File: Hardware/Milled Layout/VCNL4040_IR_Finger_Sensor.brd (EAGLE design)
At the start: 14 x 15.2 mm, 9 parts, among them U1 VCNL4040

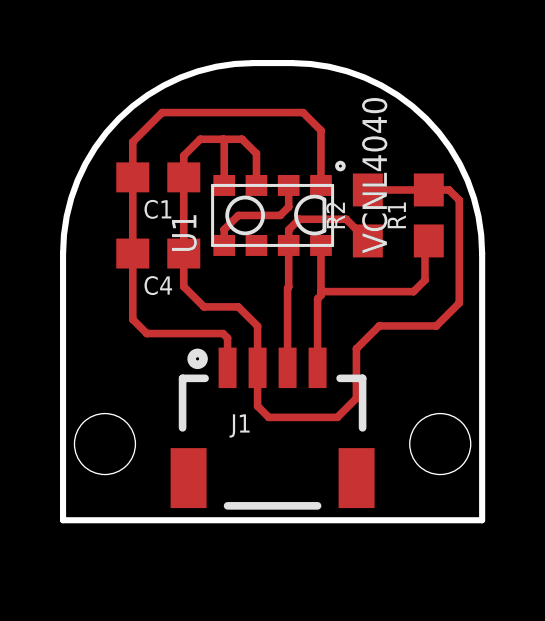
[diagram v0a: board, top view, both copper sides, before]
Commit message: Added a comparison sketch to make sure new IC works similarly to original.
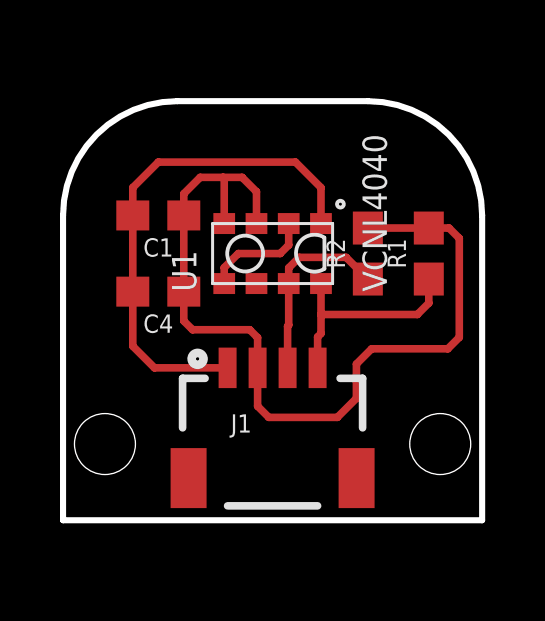
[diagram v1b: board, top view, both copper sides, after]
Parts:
- moved C4 1.27 mm to (3.17, 7.62)
- moved C1 1.27 mm to (3.17, 10.2)
- moved R1 1.27 mm to (12.2, 8.89)
- moved R2 1.27 mm to (10.2, 8.89)
- moved U1 1.27 mm to (6.99, 8.89)
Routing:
- net GND: track 19.1 -> 16.9 mm
- net SCL: track 9.15 -> 7.41 mm
- net 3.3V: track 31.5 -> 29.8 mm
- net SDA: track 7.70 -> 6.43 mm
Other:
- board size 14 x 15.2 mm -> 14 x 14 mm

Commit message: Extending PCB for molding
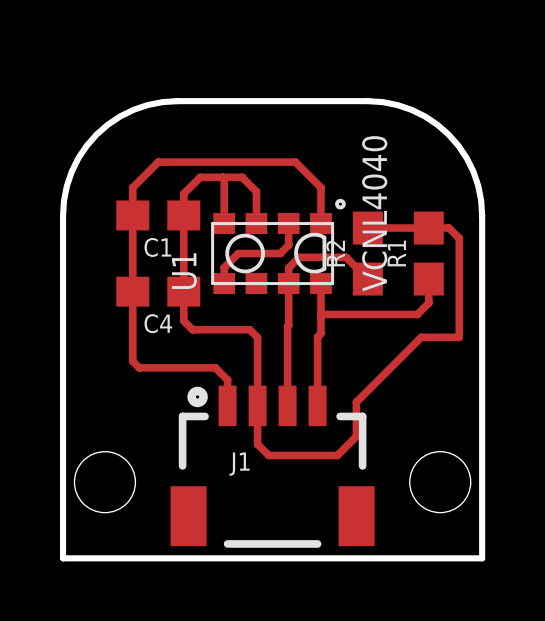
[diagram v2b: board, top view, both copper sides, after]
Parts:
- moved J1 1.27 mm to (6.99, 3.81)
- moved U$1 1.27 mm to (1.40, 1.27)
- moved U$2 1.27 mm to (12.6, 1.27)
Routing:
- net 3.3V: track 29.8 -> 31.6 mm
- net GND: track 16.9 -> 18.2 mm
- net SDA: track 6.43 -> 7.70 mm
- net SCL: track 7.41 -> 8.68 mm
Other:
- board size 14 x 14 mm -> 14 x 15.2 mm
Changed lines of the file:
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@@
 <?xml version="1.0" encoding="utf-8"?>
 <!DOCTYPE eagle SYSTEM "eagle.dtd">
-<eagle version="7.7.0">
+<eagle version="7.6.0">
 <drawing>
 <settings>
@@
 <layer number="47" name="Measures" color="7" fill="1" visible="no" active="yes"/>
 <layer number="48" name="Document" color="7" fill="1" visible="no" active="yes"/>
-<layer number="49" name="Reference" color="7" fill="1" visible="yes" active="yes"/>
+<layer number="49" name="Reference" color="7" fill="1" visible="no" active="yes"/>
 <layer number="50" name="dxf" color="7" fill="1" visible="no" active="no"/>
 <layer number="51" name="tDocu" color="6" fill="1" visible="yes" active="yes"/>
@@
 <board>
 <plain>
-<wire x1="0" y1="0" x2="13.97" y2="0" width="0.2032" layer="20"/>
-<wire x1="0" y1="0" x2="0" y2="10.16" width="0.2032" layer="20"/>
-<wire x1="13.97" y1="10.16" x2="13.97" y2="0" width="0.2032" layer="20"/>
+<wire x1="0" y1="-1.27" x2="13.97" y2="-1.27" width="0.2032" layer="20"/>
+<wire x1="0" y1="-1.27" x2="0" y2="10.16" width="0.2032" layer="20"/>
+<wire x1="13.97" y1="10.16" x2="13.97" y2="-1.27" width="0.2032" layer="20"/>
 <wire x1="10.16" y1="13.97" x2="3.81" y2="13.97" width="0.2032" layer="20"/>
 <text x="16.51" y="5.08" size="1.778" layer="51" font="vector" ratio="15">GooLine</text>
-<wire x1="0" y1="5.08" x2="13.97" y2="5.08" width="0.254" layer="51" style="shortdash"/>
+<wire x1="0" y1="3.81" x2="13.97" y2="3.81" width="0.254" layer="51" style="shortdash"/>
 <wire x1="0" y1="13.97" x2="13.97" y2="13.97" width="0.254" layer="51" style="shortdash"/>
-<wire x1="0" y1="13.97" x2="0" y2="5.08" width="0.254" layer="51" style="shortdash"/>
-<wire x1="13.97" y1="5.08" x2="13.97" y2="13.97" width="0.254" layer="51" style="shortdash"/>
+<wire x1="0" y1="13.97" x2="0" y2="3.81" width="0.254" layer="51" style="shortdash"/>
+<wire x1="13.97" y1="3.81" x2="13.97" y2="13.97" width="0.254" layer="51" style="shortdash"/>
 <dimension x1="0" y1="15.24" x2="13.97" y2="15.24" x3="6.985" y3="16.51" textsize="1.27" textratio="15" layer="47" dtype="horizontal" unit="inch"/>
 <wire x1="0" y1="10.16" x2="3.81" y2="13.97" width="0.2032" layer="20" curve="-90"/>
@@
 </element>
 <element name="U1" library="SparkX" package="VCNL4040" value="VCNL4040" x="6.985" y="8.89" rot="R90"/>
-<element name="U$1" library="SparkX" package="STAND-OFF-#2" value="STAND-OFF" x="1.397" y="2.54"/>
-<element name="U$2" library="SparkX" package="STAND-OFF-#2" value="STAND-OFF" x="12.573" y="2.54"/>
-<element name="J1" library="SparkFun-Connectors" package="1X04_1MM_RA" value="" x="6.985" y="5.08">
-<attribute name="SF_ID" value="PRT-10208" x="6.985" y="5.08" size="1.778" layer="27" font="vector" ratio="15" display="off"/>
-<attribute name="PROD_ID" value="CONN-10310" x="6.985" y="5.08" size="1.778" layer="27" font="vector" ratio="15" display="off"/>
+<element name="U$1" library="SparkX" package="STAND-OFF-#2" value="STAND-OFF" x="1.397" y="1.27"/>
+<element name="U$2" library="SparkX" package="STAND-OFF-#2" value="STAND-OFF" x="12.573" y="1.27"/>
+<element name="J1" library="SparkFun-Connectors" package="1X04_1MM_RA" value="" x="6.985" y="3.81">
+<attribute name="SF_ID" value="PRT-10208" x="6.985" y="3.81" size="1.778" layer="27" font="vector" ratio="15" display="off"/>
+<attribute name="PROD_ID" value="CONN-10310" x="6.985" y="3.81" size="1.778" layer="27" font="vector" ratio="15" display="off"/>
 </element>
 </elements>
@@
 <wire x1="3.175" y1="11.938" x2="2.325" y2="11.088" width="0.254" layer="1"/>
 <wire x1="2.325" y1="10.16" x2="2.325" y2="11.088" width="0.254" layer="1"/>
-<wire x1="5.485" y1="5.08" x2="3.048" y2="5.08" width="0.254" layer="1"/>
-<wire x1="3.048" y1="5.08" x2="2.325" y2="5.803" width="0.254" layer="1"/>
-<wire x1="2.325" y1="7.62" x2="2.325" y2="5.803" width="0.254" layer="1"/>
+<wire x1="2.325" y1="7.62" x2="2.325" y2="5.295" width="0.254" layer="1"/>
+<wire x1="2.325" y1="5.295" x2="2.54" y2="5.08" width="0.254" layer="1"/>
+<wire x1="2.54" y1="5.08" x2="5.08" y2="5.08" width="0.254" layer="1"/>
+<wire x1="5.485" y1="3.81" x2="5.485" y2="4.675" width="0.254" layer="1"/>
+<wire x1="5.485" y1="4.675" x2="5.08" y2="5.08" width="0.254" layer="1"/>
 </signal>
 <signal name="SCL">
@@
 <wire x1="8.5975" y1="6.223" x2="8.5975" y2="6.858" width="0.254" layer="1"/>
 <wire x1="8.5975" y1="6.858" x2="8.5975" y2="7.89" width="0.254" layer="1"/>
-<wire x1="8.485" y1="5.08" x2="8.485" y2="6.1105" width="0.254" layer="1"/>
+<wire x1="8.485" y1="3.81" x2="8.485" y2="6.1105" width="0.254" layer="1"/>
 <wire x1="8.485" y1="6.1105" x2="8.5975" y2="6.223" width="0.254" layer="1"/>
 <wire x1="12.192" y1="8.04" x2="12.192" y2="7.239" width="0.254" layer="1"/>
@@
 <wire x1="7.5225" y1="7.89" x2="7.5225" y2="6.5065" width="0.254" layer="1"/>
 <contactref element="J1" pad="3"/>
-<wire x1="7.485" y1="5.08" x2="7.485" y2="6.469" width="0.254" layer="1"/>
+<wire x1="7.485" y1="3.81" x2="7.485" y2="6.469" width="0.254" layer="1"/>
 <wire x1="7.485" y1="6.469" x2="7.5225" y2="6.5065" width="0.254" layer="1"/>
 <wire x1="7.5225" y1="7.89" x2="7.5225" y2="8.4115" width="0.254" layer="1"/>
@@
 <contactref element="R2" pad="2"/>
 <contactref element="U1" pad="4"/>
-<wire x1="6.858" y1="3.429" x2="9.144" y2="3.429" width="0.254" layer="1"/>
+<wire x1="6.858" y1="2.159" x2="9.144" y2="2.159" width="0.254" layer="1"/>
 <wire x1="6.4475" y1="9.89" x2="6.4475" y2="10.9515" width="0.254" layer="1"/>
 <wire x1="6.4475" y1="10.9515" x2="5.969" y2="11.43" width="0.254" layer="1"/>
@@
 <wire x1="4.025" y1="10.16" x2="4.025" y2="10.883" width="0.254" layer="1"/>
 <wire x1="4.025" y1="10.16" x2="4.025" y2="7.62" width="0.254" layer="1"/>
-<wire x1="6.485" y1="3.802" x2="6.858" y2="3.429" width="0.254" layer="1"/>
+<wire x1="6.485" y1="2.532" x2="6.858" y2="2.159" width="0.254" layer="1"/>
 <wire x1="12.192" y1="9.74" x2="12.866" y2="9.74" width="0.254" layer="1"/>
 <wire x1="12.866" y1="9.74" x2="13.208" y2="9.398" width="0.254" layer="1"/>
 <wire x1="13.208" y1="9.398" x2="13.208" y2="6.096" width="0.254" layer="1"/>
 <wire x1="10.16" y1="9.74" x2="12.192" y2="9.74" width="0.254" layer="1"/>
-<wire x1="6.485" y1="5.08" x2="6.485" y2="3.802" width="0.254" layer="1"/>
+<wire x1="6.485" y1="3.81" x2="6.485" y2="2.532" width="0.254" layer="1"/>
 <wire x1="5.3725" y1="11.3915" x2="5.334" y2="11.43" width="0.254" layer="1"/>
-<wire x1="6.485" y1="5.08" x2="6.485" y2="6.088" width="0.254" layer="1"/>
+<wire x1="6.485" y1="3.81" x2="6.485" y2="6.088" width="0.254" layer="1"/>
 <wire x1="6.485" y1="6.088" x2="6.223" y2="6.35" width="0.254" layer="1"/>
 <wire x1="6.223" y1="6.35" x2="4.318" y2="6.35" width="0.254" layer="1"/>
 <wire x1="4.318" y1="6.35" x2="4.025" y2="6.643" width="0.254" layer="1"/>
 <wire x1="4.025" y1="7.62" x2="4.025" y2="6.643" width="0.254" layer="1"/>
-<wire x1="13.208" y1="6.096" x2="12.827" y2="5.715" width="0.254" layer="1"/>
-<wire x1="12.827" y1="5.715" x2="10.287" y2="5.715" width="0.254" layer="1"/>
-<wire x1="10.287" y1="5.715" x2="9.779" y2="5.207" width="0.254" layer="1"/>
-<wire x1="9.779" y1="5.207" x2="9.779" y2="4.064" width="0.254" layer="1"/>
-<wire x1="9.779" y1="4.064" x2="9.144" y2="3.429" width="0.254" layer="1"/>
+<wire x1="9.779" y1="3.937" x2="9.779" y2="2.794" width="0.254" layer="1"/>
+<wire x1="9.779" y1="2.794" x2="9.144" y2="2.159" width="0.254" layer="1"/>
+<wire x1="13.208" y1="6.096" x2="11.938" y2="6.096" width="0.254" layer="1"/>
+<wire x1="11.938" y1="6.096" x2="9.779" y2="3.937" width="0.254" layer="1"/>
 </signal>
 <signal name="N$1">

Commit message: Moved bed back to origin
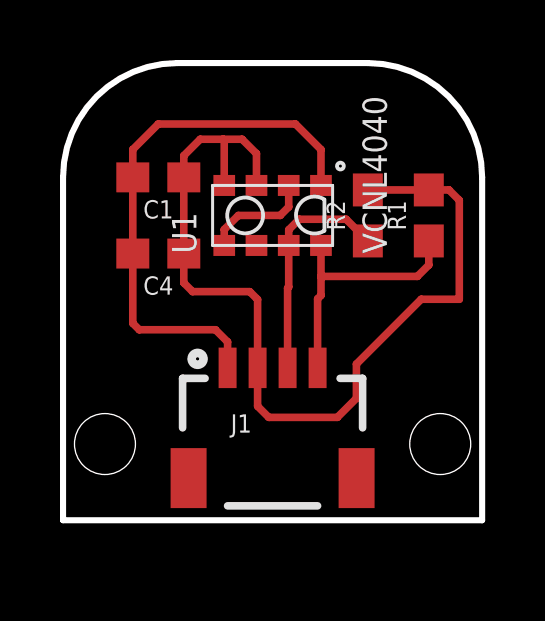
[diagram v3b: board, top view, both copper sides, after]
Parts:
- moved C4 1.27 mm to (3.17, 8.89)
- moved J1 1.27 mm to (6.99, 5.08)
- moved U$1 1.27 mm to (1.40, 2.54)
- moved U$2 1.27 mm to (12.6, 2.54)
- moved C1 1.27 mm to (3.17, 11.4)
- moved R1 1.27 mm to (12.2, 10.2)
- moved R2 1.27 mm to (10.2, 10.2)
- moved U1 1.27 mm to (6.99, 10.2)

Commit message: Adding production panel
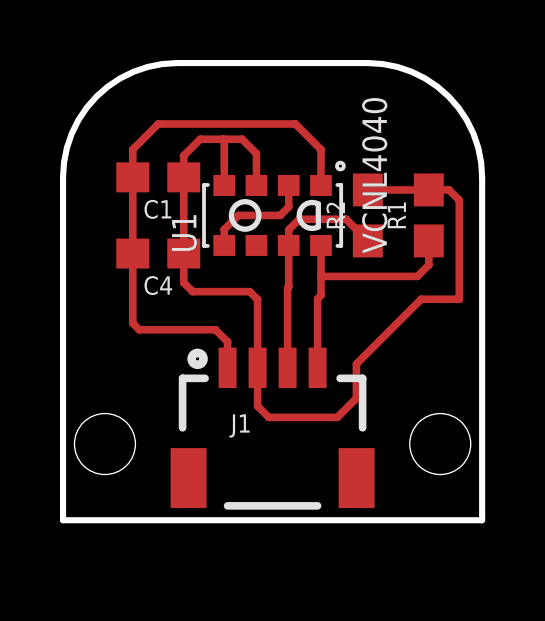
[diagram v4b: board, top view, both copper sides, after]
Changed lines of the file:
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@@
 <?xml version="1.0" encoding="utf-8"?>
 <!DOCTYPE eagle SYSTEM "eagle.dtd">
-<eagle version="7.6.0">
+<eagle version="7.7.0">
 <drawing>
 <settings>
@@
 <setting verticaltext="up"/>
 </settings>
-<grid distance="0.05" unitdist="inch" unit="mm" style="lines" multiple="1" display="yes" altdistance="0.005" altunitdist="inch" altunit="inch"/>
+<grid distance="0.05" unitdist="inch" unit="inch" style="lines" multiple="1" display="yes" altdistance="0.005" altunitdist="inch" altunit="inch"/>
 <layers>
 <layer number="1" name="Top" color="4" fill="1" visible="yes" active="yes"/>
@@
 <layer number="220" name="220bmp" color="21" fill="1" visible="no" active="no"/>
 <layer number="221" name="221bmp" color="22" fill="1" visible="no" active="no"/>
+<layer number="222" name="222bmp" color="23" fill="1" visible="no" active="no"/>
 <layer number="223" name="223bmp" color="24" fill="1" visible="no" active="no"/>
 <layer number="224" name="224bmp" color="25" fill="1" visible="no" active="no"/>
